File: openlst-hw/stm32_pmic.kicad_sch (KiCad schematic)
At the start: 18 parts, among them J14 Conn_01x03_Pin, SW1 EVP-AA602W, SW2 EVP-AA602W, U10 STM32L496RGTx

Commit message: propate the changes to RF
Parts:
- removed C58: 100nF, Capacitor_SMD:C_0402_1005Metric_Pad0.74x0.62mm_HandSolder, symbol Device:C
- removed R30: 10K, Resistor_SMD:R_0402_1005Metric_Pad0.72x0.64mm_HandSolder, symbol Device:R
- removed SW1, SW2: EVP-AA602W, Common:EVP602AA, symbol Common:EVP-AA602W
- J10: renamed from J14; Part Number (none) -> generic; now fitted
- R26: renamed from R32; value 100K -> 300K; Part Number RC0402FR-07100KL -> RC0402FR-07300KL
- renumbered R31 to R25
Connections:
- net 3V3: now also R25.1
- net VIO: no longer R25.1
- net USB/USB_OTG_FS_DM renamed USB/DN
- net USB/USB_OTG_FS_DP renamed USB/DP
- no-connect marks 24 -> 20
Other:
- added sheet BOOT (../avionics_board/boot.kicad_sch)
- added sheet RESET (../sci_board/reset.kicad_sch)
- sheet USB ports: added DN, DP, GND, VBUS1, VBUS2; removed GND1, GND2, USB_OTG_FS_DM, USB_OTG_FS_DP, VUSB1, VUSB2

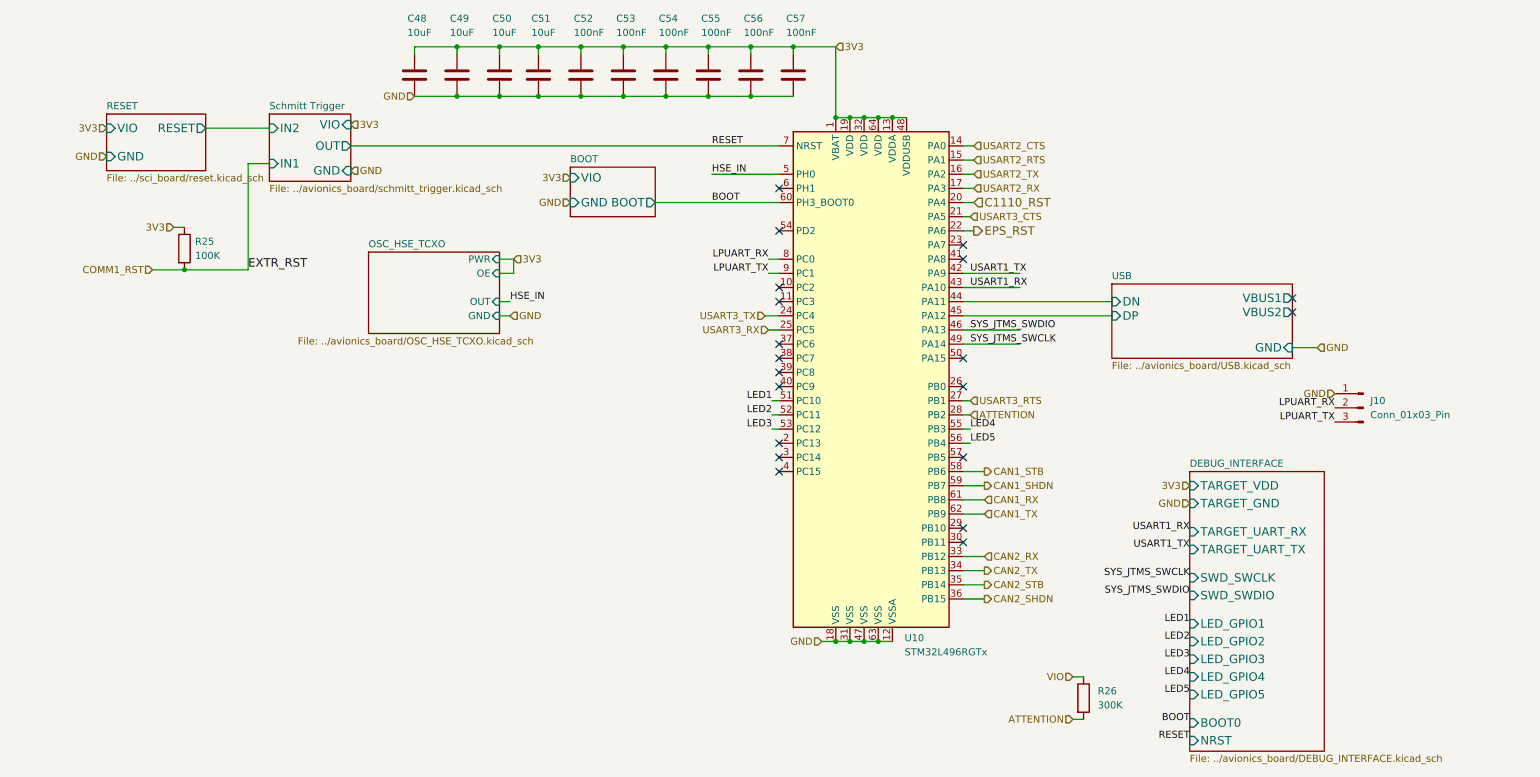
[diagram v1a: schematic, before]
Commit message: local switches and monitors for SCI and RF
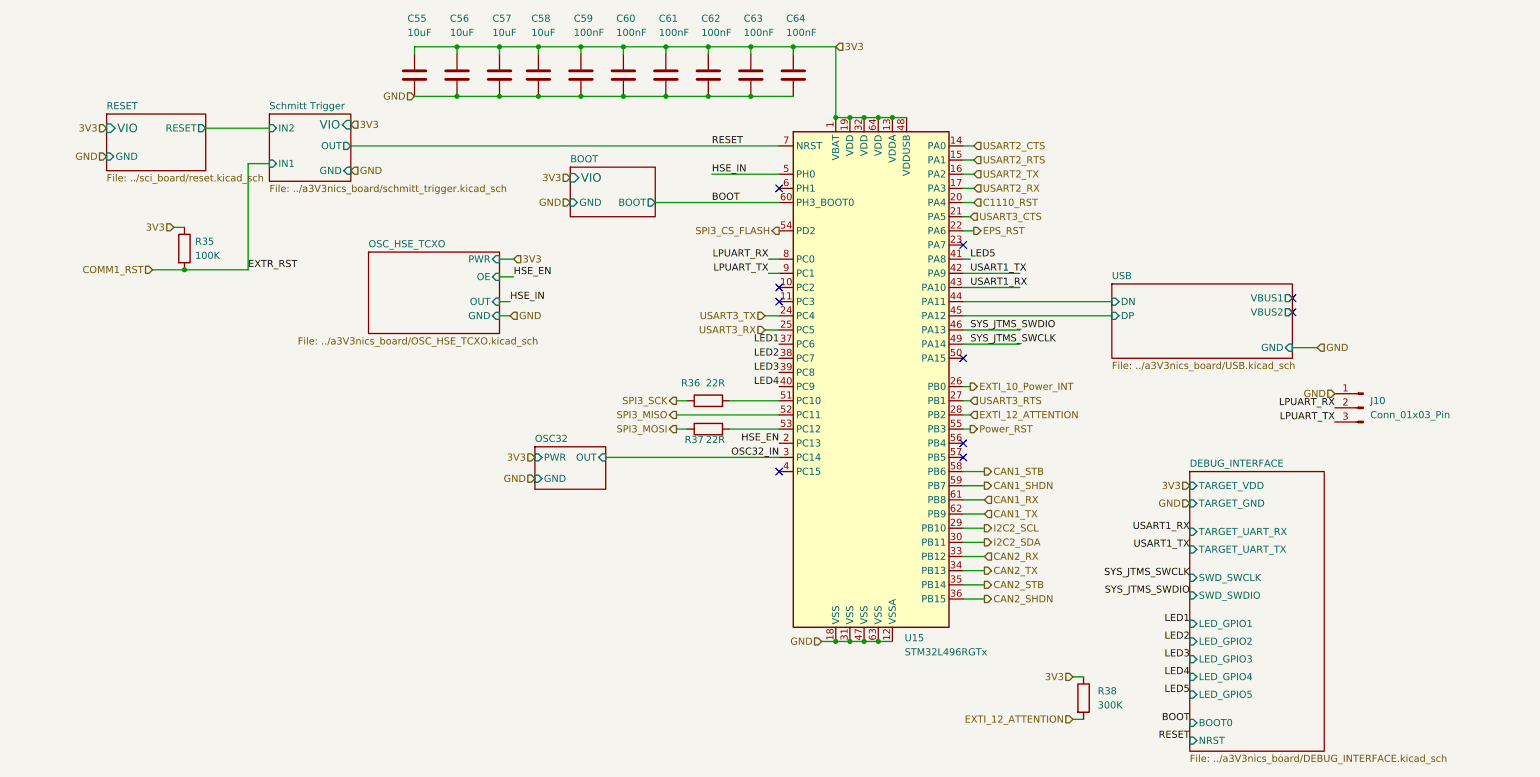
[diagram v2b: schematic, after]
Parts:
- added R36, R37: 22R, Resistor_SMD:R_0402_1005Metric_Pad0.72x0.64mm_HandSolder, symbol Device:R
- renumbered C48 to C55, C49 to C56, C50 to C57, C51 to C58, C52 to C59, C53 to C60, C54 to C61, C55 to C62, C56 to C63, C57 to C64, R25 to R35, R26 to R38, U10 to U15
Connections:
- net VIO is gone; now on net 3V3: R38.1
- net LED1: now also U15.37 (PC6); no longer U15.51 (PC10)
- net LED2: now also U15.38 (PC7); no longer U15.52 (PC11)
- net LED3: now also U15.39 (PC8); no longer U15.53 (PC12)
- net LED4: now also U15.40 (PC9); no longer U15.55 (PB3)
- net LED5: now also U15.41 (PA8); no longer U15.56 (PB4)
- net HSE_EN: now reaches U15.2 (PC13)
- net EXTI_10_Power_INT: now reaches U15.26 (PB0)
- net I2C2_SCL: now reaches U15.29 (PB10)
- net OSC32_IN: now reaches U15.3 (PC14)
- net I2C2_SDA: now reaches U15.30 (PB11)
- net SPI3_CS_FLASH: now reaches U15.54 (PD2)
- net ATTENTION renamed EXTI_12_ATTENTION
- new net: R37.2, U15.53 (PC12)
- new net: R36.2, U15.51 (PC10)
- new net Power_RST: U15.55 (PB3)
- new net SPI3_MISO: U15.52 (PC11)
- new net SPI3_MOSI: R37.1
- new net SPI3_SCK: R36.1
- no-connect marks 20 -> 10
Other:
- added sheet OSC32 (../avionics_board/OSC32_TCXO.kicad_sch)
- sheet DEBUG_INTERFACE: file ../avionics_board/DEBUG_INTERFACE.kicad_sch -> ../a3V3nics_board/DEBUG_INTERFACE.kicad_sch
- sheet OSC_HSE_TCXO: file ../avionics_board/OSC_HSE_TCXO.kicad_sch -> ../a3V3nics_board/OSC_HSE_TCXO.kicad_sch
- sheet Schmitt Trigger: file ../avionics_board/schmitt_trigger.kicad_sch -> ../a3V3nics_board/schmitt_trigger.kicad_sch
- sheet USB: file ../avionics_board/USB.kicad_sch -> ../a3V3nics_board/USB.kicad_sch
